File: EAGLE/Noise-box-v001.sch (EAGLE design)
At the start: 76 parts, among them J1 AVR_SPI_PROG_3X22X3_LOCK, J4 MICRO-SD_CARD_SOCKET, J5 HEADPHONE, J6 POWER_JACK, U1 ATMEGA328P_TQFP, U2 MIC5219 3.3V, U3 MCP73831, Y1 12.288MHz, Y2 8MHz

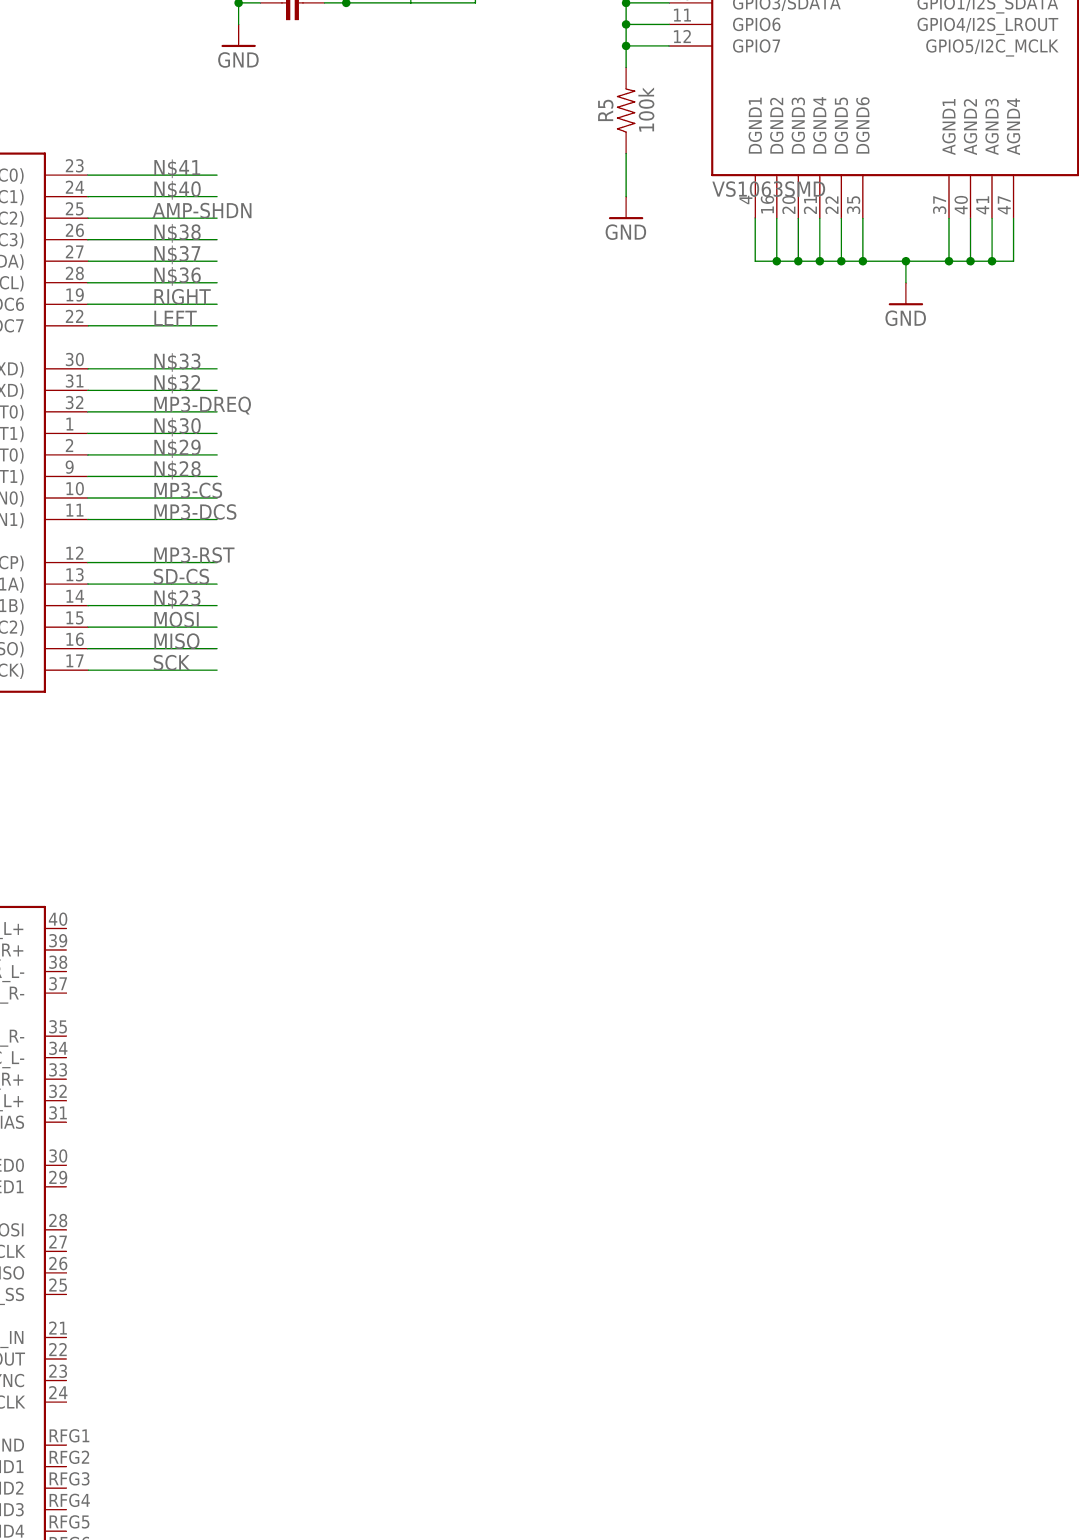
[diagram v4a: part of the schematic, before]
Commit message: Triggers
Added momentary buttons to act as triggers. These will choose between
music categories, songs, or other user input features.
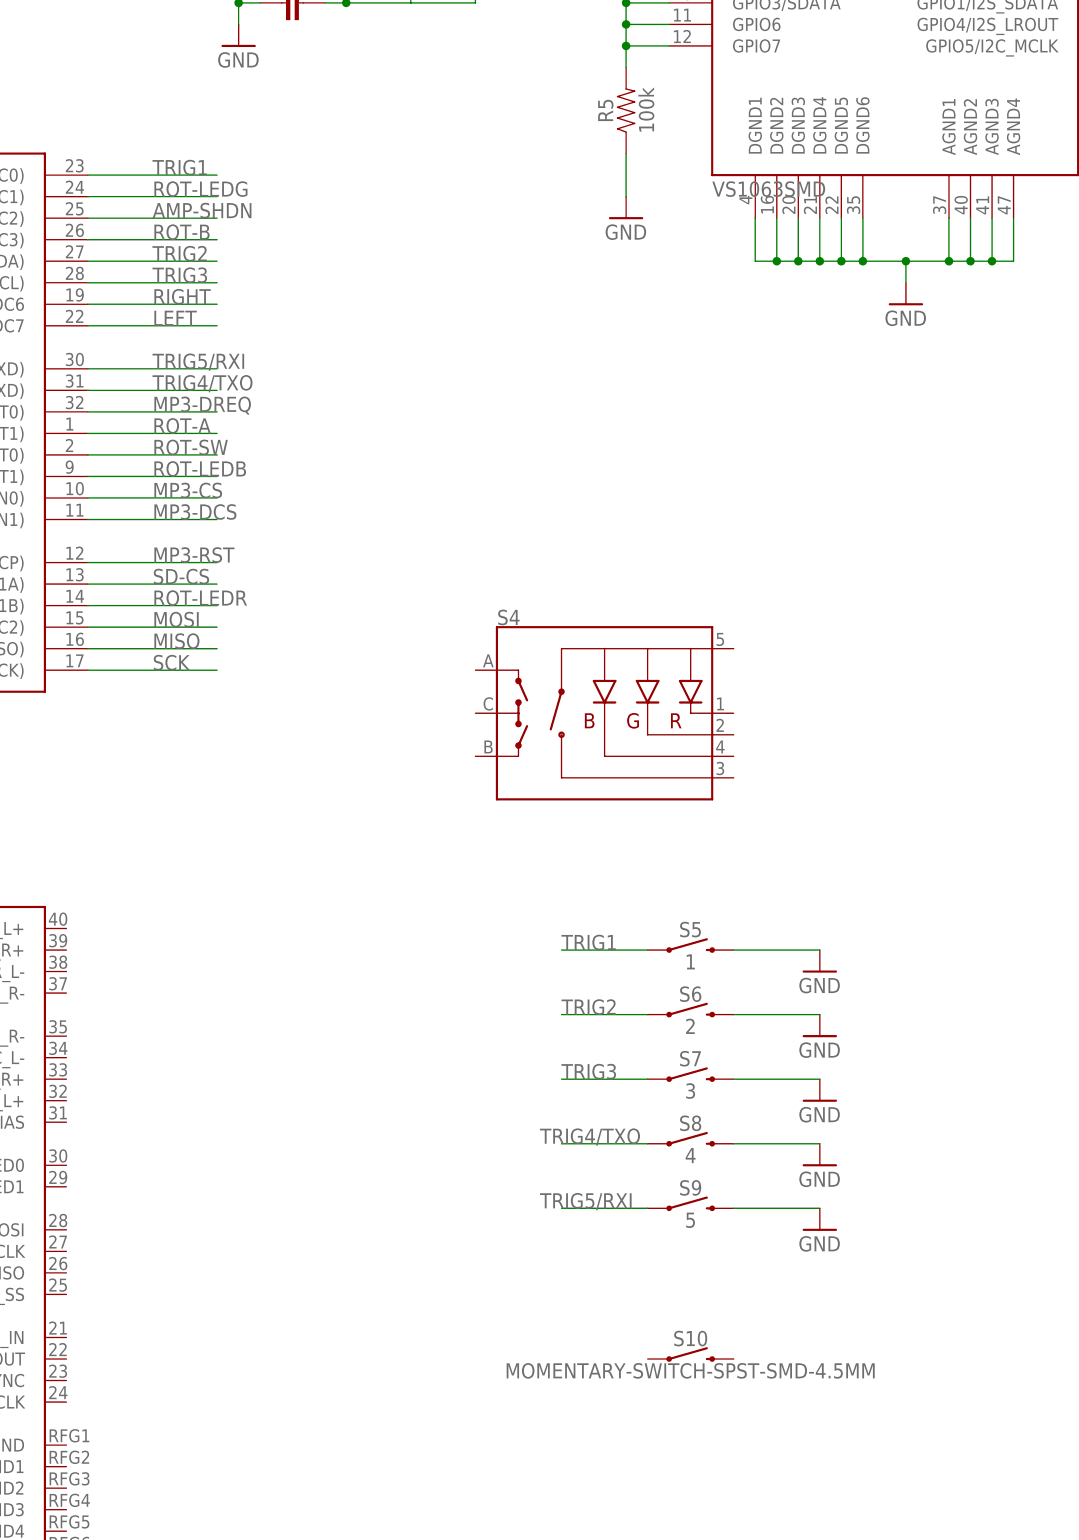
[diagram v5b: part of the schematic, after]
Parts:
- added S10: MOMENTARY-SWITCH-SPST-SMD-4.5MM, SparkFun-Switches:MOMENTARY-SWITCH-SPST-SMD-4.5MM
- added S4: (no value), SparkFun-Switches:ENCODER-RGB-SWITCH
- added S5: 1, SparkFun-Switches:MOMENTARY-SWITCH-SPST-SMD-4.5MM
- added S6: 2, SparkFun-Switches:MOMENTARY-SWITCH-SPST-SMD-4.5MM
- added S7: 3, SparkFun-Switches:MOMENTARY-SWITCH-SPST-SMD-4.5MM
- added S8: 4, SparkFun-Switches:MOMENTARY-SWITCH-SPST-SMD-4.5MM
- added S9: 5, SparkFun-Switches:MOMENTARY-SWITCH-SPST-SMD-4.5MM
- S2, S3: device SparkFun-Switches:MOMENTARY-SWITCH-SPST-PTH-6.0MM -> SparkFun-Switches:MOMENTARY-SWITCH-SPST-SMD-4.5MM
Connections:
- net N$23 renamed ROT-LEDR
- net N$28 renamed ROT-LEDB
- net N$29 renamed ROT-SW
- net N$30 renamed ROT-A
- net N$38 renamed ROT-B
- net N$40 renamed ROT-LEDG
- removed net N$32: U1.PD1(TXD)
- removed net N$33: U1.PD0(RXD)
- removed net N$36: U1.PC5(ADC5/SCL)
- removed net N$37: U1.PC4(ADC4/SDA)
- removed net N$41: U1.PC0(ADC0)
- new net TRIG1: S5.1, U1.PC0(ADC0)
- new net TRIG2: S6.1, U1.PC4(ADC4/SDA)
- new net TRIG3: S7.1, U1.PC5(ADC5/SCL)
- new net TRIG4/TXO: S8.1, U1.PD1(TXD)
- new net TRIG5/RXI: S9.1, U1.PD0(RXD)
- net GND: now also S5.2, S6.2, S7.2, S8.2, S9.2
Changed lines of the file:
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@@
 <part name="C26" library="SparkFun-Capacitors" deviceset="0.1UF" device="-0603-25V-5%" value="0.1uF"/>
 <part name="C27" library="SparkFun-Capacitors" deviceset="0.1UF" device="-0603-25V-5%" value="0.1uF"/>
-<part name="S2" library="SparkFun-Switches" deviceset="MOMENTARY-SWITCH-SPST" device="-PTH-6.0MM" value="UP"/>
-<part name="S3" library="SparkFun-Switches" deviceset="MOMENTARY-SWITCH-SPST" device="-PTH-6.0MM" value="DOWN"/>
+<part name="S2" library="SparkFun-Switches" deviceset="MOMENTARY-SWITCH-SPST" device="-SMD-4.5MM" value="UP"/>
+<part name="S3" library="SparkFun-Switches" deviceset="MOMENTARY-SWITCH-SPST" device="-SMD-4.5MM" value="DOWN"/>
 <part name="GND29" library="supply1" deviceset="GND" device=""/>
 <part name="GND30" library="supply1" deviceset="GND" device=""/>
@@
 <part name="R18" library="SparkFun-Resistors" deviceset="10KOHM" device="-0603-1/10W-1%" value="10k"/>
 <part name="+3V14" library="supply1" deviceset="+3V3" device=""/>
+<part name="S4" library="SparkFun-Switches" deviceset="ENCODER-RGB-SWITCH" device=""/>
+<part name="S5" library="SparkFun-Switches" deviceset="MOMENTARY-SWITCH-SPST" device="-SMD-4.5MM" value="1"/>
+<part name="S6" library="SparkFun-Switches" deviceset="MOMENTARY-SWITCH-SPST" device="-SMD-4.5MM" value="2"/>
+<part name="S7" library="SparkFun-Switches" deviceset="MOMENTARY-SWITCH-SPST" device="-SMD-4.5MM" value="3"/>
+<part name="S8" library="SparkFun-Switches" deviceset="MOMENTARY-SWITCH-SPST" device="-SMD-4.5MM" value="4"/>
+<part name="S9" library="SparkFun-Switches" deviceset="MOMENTARY-SWITCH-SPST" device="-SMD-4.5MM" value="5"/>
+<part name="S10" library="SparkFun-Switches" deviceset="MOMENTARY-SWITCH-SPST" device="-SMD-4.5MM"/>
+<part name="GND33" library="supply1" deviceset="GND" device=""/>
+<part name="GND34" library="supply1" deviceset="GND" device=""/>
+<part name="GND35" library="supply1" deviceset="GND" device=""/>
+<part name="GND36" library="supply1" deviceset="GND" device=""/>
+<part name="GND37" library="supply1" deviceset="GND" device=""/>
 </parts>
 <sheets>
@@
 <instance part="R18" gate="G$1" x="187.96" y="203.2" rot="R90"/>
 <instance part="+3V14" gate="G$1" x="187.96" y="213.36"/>
+<instance part="S4" gate="G$1" x="312.42" y="132.08"/>
+<instance part="S5" gate="G$1" x="322.58" y="104.14"/>
+<instance part="S6" gate="G$1" x="322.58" y="96.52"/>
+<instance part="S7" gate="G$1" x="322.58" y="88.9"/>
+<instance part="S8" gate="G$1" x="322.58" y="81.28"/>
+<instance part="S9" gate="G$1" x="322.58" y="73.66"/>
+<instance part="S10" gate="G$1" x="322.58" y="55.88"/>
+<instance part="GND33" gate="1" x="337.82" y="93.98"/>
+<instance part="GND34" gate="1" x="337.82" y="101.6"/>
+<instance part="GND35" gate="1" x="337.82" y="86.36"/>
+<instance part="GND36" gate="1" x="337.82" y="78.74"/>
+<instance part="GND37" gate="1" x="337.82" y="71.12"/>
 </instances>
 <busses>
@@
 <pinref part="GND32" gate="1" pin="GND"/>
 </segment>
+<segment>
+<pinref part="S5" gate="G$1" pin="2"/>
+<wire x1="327.66" y1="104.14" x2="337.82" y2="104.14" width="0.1524" layer="91"/>
+<pinref part="GND34" gate="1" pin="GND"/>
+</segment>
+<segment>
+<pinref part="S6" gate="G$1" pin="2"/>
+<wire x1="327.66" y1="96.52" x2="337.82" y2="96.52" width="0.1524" layer="91"/>
+<pinref part="GND33" gate="1" pin="GND"/>
+</segment>
+<segment>
+<pinref part="S7" gate="G$1" pin="2"/>
+<wire x1="327.66" y1="88.9" x2="337.82" y2="88.9" width="0.1524" layer="91"/>
+<pinref part="GND35" gate="1" pin="GND"/>
+</segment>
+<segment>
+<pinref part="S8" gate="G$1" pin="2"/>
+<wire x1="327.66" y1="81.28" x2="337.82" y2="81.28" width="0.1524" layer="91"/>
+<pinref part="GND36" gate="1" pin="GND"/>
+</segment>
+<segment>
+<pinref part="S9" gate="G$1" pin="2"/>
+<wire x1="327.66" y1="73.66" x2="337.82" y2="73.66" width="0.1524" layer="91"/>
+<pinref part="GND37" gate="1" pin="GND"/>
+</segment>
 </net>
 <net name="MOSI" class="0">
@@
 </segment>
 </net>
-<net name="N$23" class="0">
+<net name="ROT-LEDR" class="0">
 <segment>
 <pinref part="U1" gate="U$1" pin="PB2(SS/OC1B)"/>
@@
 </segment>
 </net>
-<net name="N$28" class="0">
+<net name="ROT-LEDB" class="0">
 <segment>
 <pinref part="U1" gate="U$1" pin="PD5(T1)"/>
@@
 </segment>
 </net>
-<net name="N$29" class="0">
+<net name="ROT-SW" class="0">
 <segment>
 <pinref part="U1" gate="U$1" pin="PD4(XCK/T0)"/>
@@
 </segment>
 </net>
-<net name="N$30" class="0">
+<net name="ROT-A" class="0">
 <segment>
 <pinref part="U1" gate="U$1" pin="PD3(INT1)"/>
@@
 </segment>
 </net>
-<net name="N$32" class="0">
+<net name="TRIG4/TXO" class="0">
 <segment>
 <pinref part="U1" gate="U$1" pin="PD1(TXD)"/>
@@
 <label x="259.08" y="170.18" size="1.778" layer="95"/>
 </segment>
-</net>
-<net name="N$33" class="0">
+<segment>
+<pinref part="S8" gate="G$1" pin="1"/>
+<wire x1="317.5" y1="81.28" x2="307.34" y2="81.28" width="0.1524" layer="91"/>
+<label x="304.8" y="81.28" size="1.778" layer="95"/>
+</segment>
+</net>
+<net name="TRIG5/RXI" class="0">
 <segment>
 <pinref part="U1" gate="U$1" pin="PD0(RXD)"/>
@@
 <label x="259.08" y="172.72" size="1.778" layer="95"/>
 </segment>
-</net>
-<net name="N$36" class="0">
+<segment>
+<pinref part="S9" gate="G$1" pin="1"/>
+<wire x1="317.5" y1="73.66" x2="307.34" y2="73.66" width="0.1524" layer="91"/>
+<label x="304.8" y="73.66" size="1.778" layer="95"/>
+</segment>
+</net>
+<net name="TRIG3" class="0">
 <segment>
 <pinref part="U1" gate="U$1" pin="PC5(ADC5/SCL)"/>
@@
 <label x="259.08" y="182.88" size="1.778" layer="95"/>
 </segment>
-</net>
-<net name="N$37" class="0">
+<segment>
+<pinref part="S7" gate="G$1" pin="1"/>
+<wire x1="317.5" y1="88.9" x2="307.34" y2="88.9" width="0.1524" layer="91"/>
+<label x="307.34" y="88.9" size="1.778" layer="95"/>
+</segment>
+</net>
+<net name="TRIG2" class="0">
 <segment>
 <pinref part="U1" gate="U$1" pin="PC4(ADC4/SDA)"/>
@@
 <label x="259.08" y="185.42" size="1.778" layer="95"/>
 </segment>
-</net>
-<net name="N$38" class="0">
+<segment>
+<pinref part="S6" gate="G$1" pin="1"/>
+<wire x1="317.5" y1="96.52" x2="307.34" y2="96.52" width="0.1524" layer="91"/>
+<label x="307.34" y="96.52" size="1.778" layer="95"/>
+</segment>
+</net>
+<net name="ROT-B" class="0">
 <segment>
 <pinref part="U1" gate="U$1" pin="PC3(ADC3)"/>
@@
 </segment>
 </net>
-<net name="N$40" class="0">
+<net name="ROT-LEDG" class="0">
 <segment>
 <pinref part="U1" gate="U$1" pin="PC1(ADC1)"/>
@@
 </segment>
 </net>
-<net name="N$41" class="0">
+<net name="TRIG1" class="0">
 <segment>
 <pinref part="U1" gate="U$1" pin="PC0(ADC0)"/>
@@
 <label x="259.08" y="195.58" size="1.778" layer="95"/>
 </segment>
-</net>
+<segment>
+<pinref part="S5" gate="G$1" pin="1"/>
+<wire x1="317.5" y1="104.14" x2="307.34" y2="104.14" width="0.1524" layer="91"/>
+<label x="307.34" y="104.14" size="1.778" layer="95"/>
+</segment>
+</net>
